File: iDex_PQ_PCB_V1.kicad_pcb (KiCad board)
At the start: 2 copper layers, 170.8 x 83.1 mm, 172 parts, among them J1 Conn_01x02, J10 Conn_01x03_Pin, J12 Conn_01x06_Pin, J13 Conn_01x08_Pin, J14 Conn_01x08_Pin, J15 Conn_01x08_Pin, J16 Conn_01x08_Pin, J17 Conn_01x08_Pin, J18 Conn_01x08_Pin, J19 Conn_01x03_Pin, J2 Barrel_Jack_Switch_Pin3Ring, J20 Conn_01x03_Pin, J21 Conn_01x03_Pin, J22 Conn_01x03_Pin, J23 Conn_01x03_Pin, J3 Conn_01x05, J4 Conn_01x02, J5 Conn_01x02, J6 Conn_01x02, J7 Conn_01x02, J8 Screw_Terminal_01x04, J9 Conn, Q1 BC847, Q2 BC847, Q3 BC847, SW1 SW_SPDT, SW2 SW_MEC_5E, SW3 SW_MEC_5E, U1 ADE9430ACPZ, U2 STM32H7R3V8Tx, U3 AMS1117-3.3, U4 AMS1117-3.3, Y1 8MHz, Y2 32.768KHz, Y4 24.576MHz

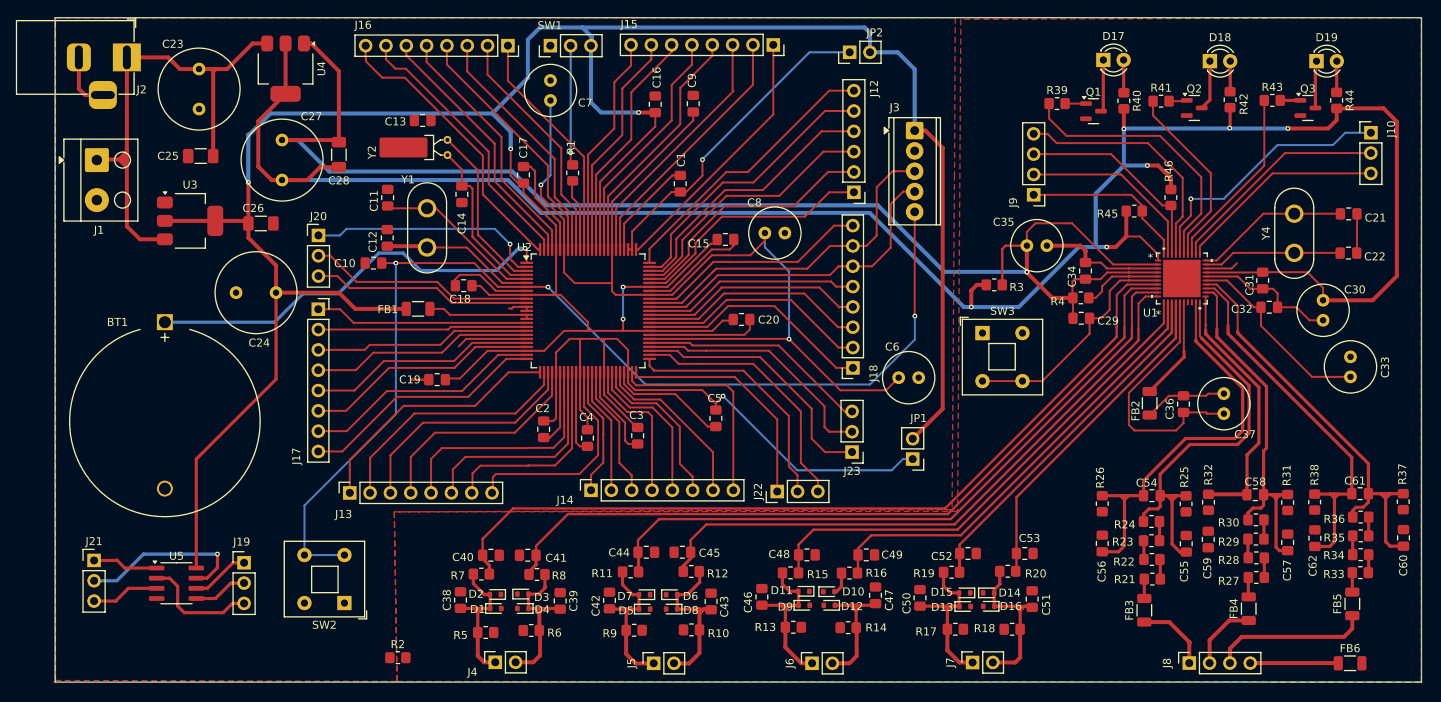
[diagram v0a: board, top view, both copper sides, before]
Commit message: Bottom Layer Plane Added
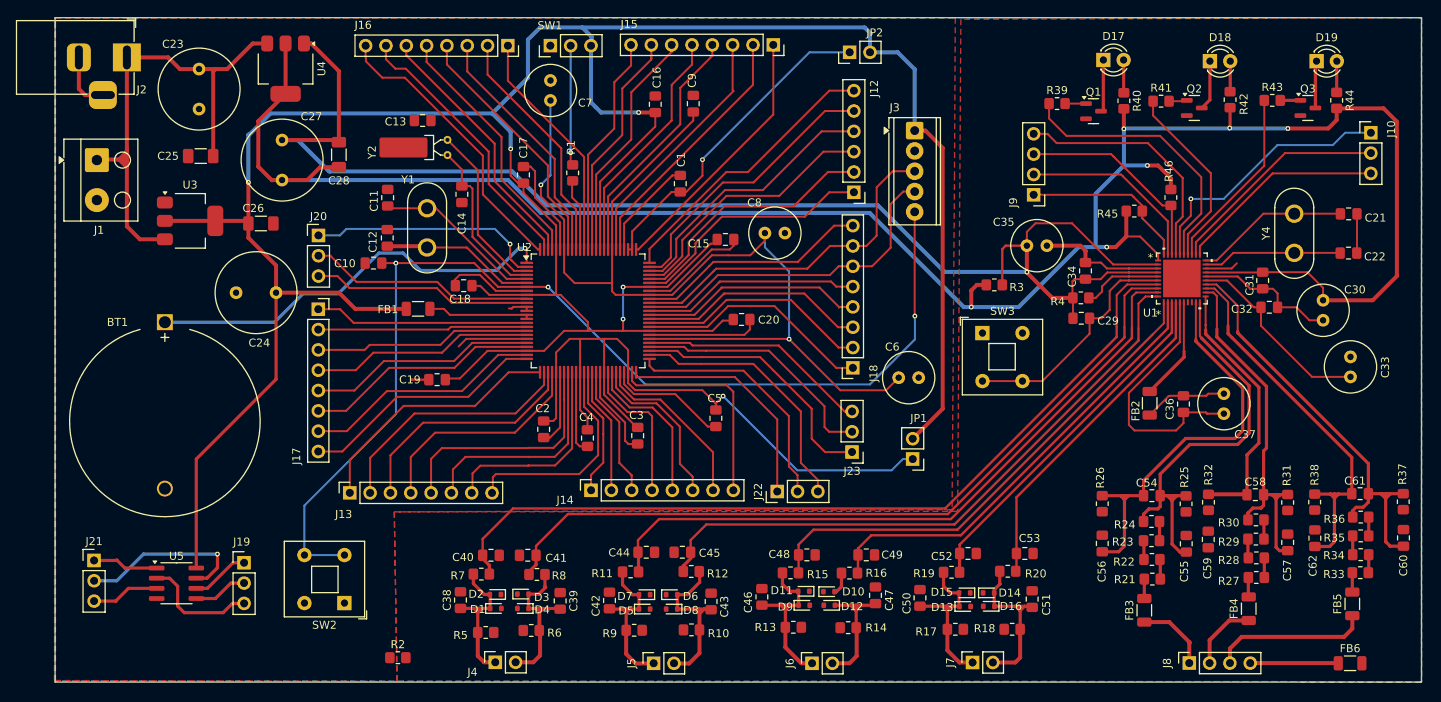
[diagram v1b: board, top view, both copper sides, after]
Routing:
- added copper zone on B.Cu, net GND
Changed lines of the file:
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@@
 			(outputformat 1)
 			(mirror no)
-			(drillshape 1)
+			(drillshape 0)
 			(scaleselection 1)
-			(outputdirectory "")
+			(outputdirectory "C:/DEE/iDEX/iDex_STM32_Main_PCB/Gerber/")
 		)
 	)
@@
 			)
 		)
+	)
+	(zone
+		(net 1)
+		(net_name "GND")
+		(layer "B.Cu")
+		(hatch edge 0.5)
+		(priority 2)
+		(connect_pads
+			(clearance 0.25)
+		)
+		(min_thickness 0.25)
+		(filled_areas_thickness no)
+		(fill yes
+			(thermal_gap 0.5)
+			(thermal_bridge_width 0.5)
+		)
+		(polygon
+			(pts
+				(xy 33.1 25.6) (xy 203.9 25.6) (xy 203.9 108.6) (xy 33 108.5)
+			)
+		)

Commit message: Changes done as per Poineer Circuits
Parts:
- added D20: LED, LED_SMD:LED_0805_2012Metric_Pad1.15x1.40mm_HandSolder, F.Cu at (37.9, 61.7)
- added D21: LED, LED_SMD:LED_0805_2012Metric_Pad1.15x1.40mm_HandSolder, F.Cu at (156.8, 29.8)
- added J11: Conn_01x02, Connector_PinSocket_2.54mm:PinSocket_1x02_P2.54mm_Vertical, F.Cu at (141.9, 28.0)
- added R47: 4.7K, Resistor_SMD:R_0805_2012Metric_Pad1.20x1.40mm_HandSolder, F.Cu at (38.0, 56.6)
- added R48: 4.7K, Resistor_SMD:R_0805_2012Metric_Pad1.20x1.40mm_HandSolder, F.Cu at (151.4, 29.8)
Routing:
- net +3.3V: track 375.1 -> 405.3 mm
- net +ADE_3.3V: track 270.0 -> 299.6 mm
- net GND: track 132.2 -> 142.4 mm, vias 0 -> 14
- net /ADE9430_Schematic/VBN: track 33.0 -> 41.0 mm
- net /ADE9430_Schematic/IAP: track 105.4 -> 111.1 mm
- net Net-(U2-PC14): track 21.4 -> 25.1 mm
- net Net-(D21-A): track 0.00 -> 3.38 mm
- net ADE_GND: track 235.7 -> 238.9 mm, vias 1 -> 20
- net Net-(D20-A): track 0.00 -> 3.12 mm
- net /STM32_Schematic/91: track 30.1 -> 32.3 mm
- net Net-(D10-A): track 19.7 -> 21.4 mm
- net /ADE9430_Schematic/IAN: track 98.1 -> 98.8 mm
- added copper zone on B.Cu, net ADE_GND
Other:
- board text added: "10"
- board text added: "100"
- board text added: "11"
- board text added: "16"
- board text added: "17"
- board text added: "18"
- board text added: "19"
- board text added: "2"
- board text added: "21"
- board text added: "22"
- board text added: "24"
- board text added: "25"
- board text added: "26"
- board text added: "27"
- board text added: "28"
- board text added: "29"
- board text added: "32"
- board text added: "33"
- board text added: "34"
- board text added: "37"
- board text added: "38"
- board text added: "39"
- board text added: "40"
- board text added: "43"
- board text added: "44"
- board text added: "45"
- board text added: "46"
- board text added: "49"
- board text added: "53"
- board text added: "54"
- board text added: "55"
- board text added: "59"
- board text added: "60"
- board text added: "61"
- board text added: "62"
- board text added: "63"
- board text added: "64"
- board text added: "65"
- board text added: "66"
- board text added: "70"
- board text added: "71"
- board text added: "72"
- board text added: "73"
- board text added: "74"
- board text added: "75"
- board text added: "76"
- board text added: "80"
- board text added: "81"
- board text added: "83"
- board text added: "84"
- board text added: "86"
- board text added: "87"
- board text added: "88"
- board text added: "89"
- board text added: "91"
- board text added: "92"
- board text added: "93"
- board text added: "97"
- board text added: "98"
- board text added: "99"
- board text added: "BOT"
- board text added: "Idex_PCB_V1.0"
- board text added: "TOP"
- board text added: "VDD_SPI"
- board text added: "VDD_USB"

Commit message: Voltage Foot print changed
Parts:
- J8: footprint Connector_PinSocket_2.54mm:PinSocket_1x04_P2.54mm_Vertical -> TerminalBlock:TerminalBlock_MaiXu_MX126-5.0-04P_1x04_P5.00mm
- moved J8 2.11 mm to (173.7, 104.5), turned to 0 degrees
- moved FB4 1.69 mm to (183.5, 98.3), turned to 180 degrees
- moved FB3 1.68 mm to (170.5, 98.6), turned to 180 degrees
- moved FB5 1.66 mm to (196.4, 97.7), turned to 180 degrees
- moved FB6 1.32 mm to (195.5, 105.1)
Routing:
- net /ADE9430_Schematic/Voltage_Current_Channels/N: track 11.0 -> 5.57 mm
- net /ADE9430_Schematic/Voltage_Current_Channels/V_R: track 9.32 -> 6.60 mm
- net /ADE9430_Schematic/Voltage_Current_Channels/V_B: track 19.8 -> 18.4 mm
- net /ADE9430_Schematic/Voltage_Current_Channels/V_Y: track 8.77 -> 9.44 mm

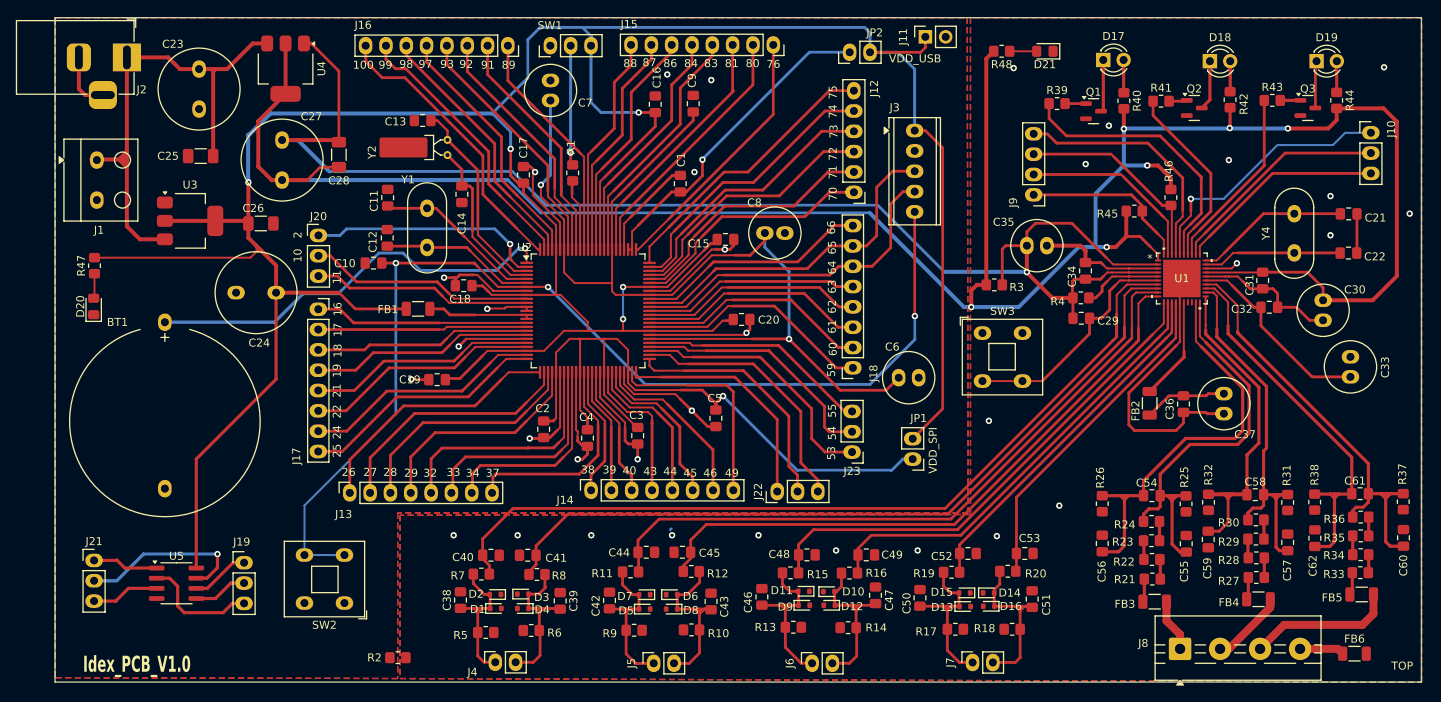
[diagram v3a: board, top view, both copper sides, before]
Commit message: track width changed
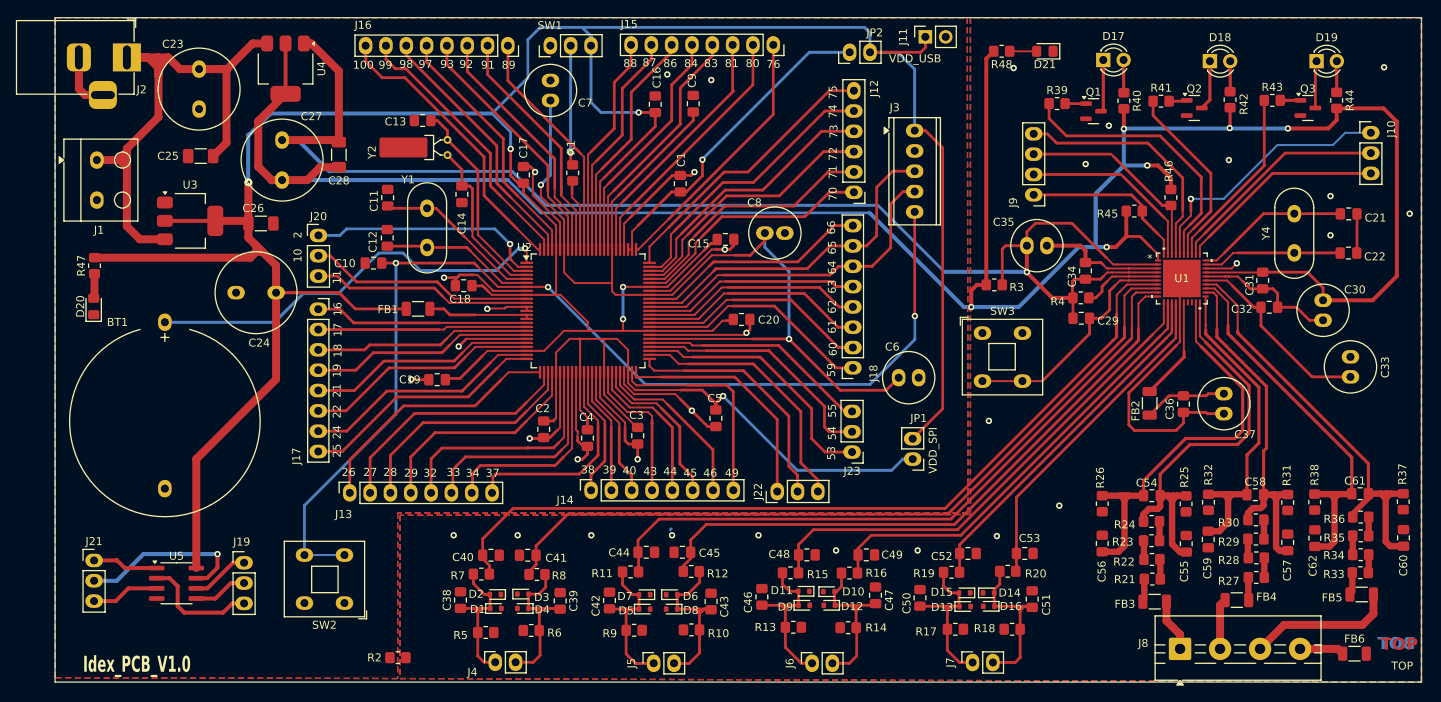
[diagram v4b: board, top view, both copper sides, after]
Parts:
- moved FB4 2.70 mm to (180.8, 98.4), turned to 0 degrees
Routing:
- net Net-(J1-Pin_1): track 65.8 -> 76.0 mm
- net /ADE9430_Schematic/Voltage_Current_Channels/V_Y: track 9.44 -> 6.36 mm
- net GND: track 142.4 -> 144.3 mm
- net /ADE9430_Schematic/VCP: track 54.2 -> 53.7 mm

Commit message: Kumaravel
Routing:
- net ADE_GND: track 238.9 -> 231.2 mm
- net +3.3V: track 405.3 -> 410.8 mm
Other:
- board text added: "iDEX-PQM_V1.0"
- board text removed: "Idex_PCB_V1.0"
